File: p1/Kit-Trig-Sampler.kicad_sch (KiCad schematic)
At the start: 84 parts, among them J1 START_CV, J10 AUDIO_INR, J11 AUDIO_OUTL, J13 BANK_CV, J14 Eurorack_Power_16pin_Unshroud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, J2 LENGTH_CV, J3 SAMP_CV, J4 PITCH CV, J5 REV_TRIG, J6 PLAY_TRIG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

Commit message: changes to schem and layout
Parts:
- removed C19: 10uF_Radial_TH, 4ms_Capacitor:CP_Radial_P2.5mm, symbol 4ms_Capacitor:10uF_Radial_TH
- removed R9: 620Ω_TH0.125, 4ms_Resistor:R_Axial_DIN0207_L6.3mm_D2.5mm_P7.62mm_Horizontal, symbol 4ms_Resistor_TH:620Ω_TH0.125
- added C19: 47uF_16V_TH, 4ms_Capacitor:CP_Radial_P2.5mm, symbol 4ms_Capacitor:47uF_16V_TH
- added R35: 33k_TH0.125, 4ms_Resistor:R_Axial_DIN0207_L6.3mm_D2.5mm_P7.62mm_Horizontal, symbol 4ms_Resistor_TH:33k_TH0.125
- added R37, R9: 10k_TH0.125, 4ms_Resistor:R_Axial_DIN0207_L6.3mm_D2.5mm_P7.62mm_Horizontal, symbol 4ms_Resistor_TH:10k_TH0.125
- added unit 2 of U2
- R11: symbol 4ms_Resistor_TH:1k_TH0.125 -> 4ms_Resistor_TH:33k_TH0.125; Display 1k -> 33k; Part Number 299-1k-RC -> 299-33k-RC; Specifications 1k, 5%, 1/8W, TH0.125 -> 33k, 5%, 1/8W, TH0.125
- R13: symbol 4ms_Resistor_TH:68k_TH0.125 -> 4ms_Resistor_TH:33k_TH0.125; Display 68k -> 33k; Part Number 299-68k-RC -> 299-33k-RC; Specifications 68k, 5%, 1/8W, TH0.125 -> 33k, 5%, 1/8W, TH0.125
- R25, R26, R27: value 4.7k_TH0.125 -> 10k_TH0.125; symbol 4ms_Resistor_TH:4.7k_TH0.125 -> 4ms_Resistor_TH:10k_TH0.125; Display 4.7k -> 10k; Part Number 299-4.7k-RC -> 299-10k-RC; Specifications 4.7k, 5%, 1/8W, TH0.125 -> 10k, 5%, 1/8W, TH0.125
- U3: footprint Package_TO_SOT_THT:TO-220-3_Vertical -> 4ms_Package_TO:TO-220-3_PXO7803
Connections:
- net +12V: now also C19.1
- net GND: now also C19.2, R35.1, R9.1, U2.5 (+); no longer R13.1
- net at C3.2, R11.1, U1.5 (+): now also R37.2
- new net: R37.1, R9.2
- new net: R13.1, R35.2
- new net: U2.6 (-), U2.7
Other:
- note added: "4ms Sampler Kit"
- note removed: "4ms STS Kit"
- moved on the sheet: Bank_But1, C1, C10, C11, C12, C13, C14, C15, C16, C17, C18, C2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

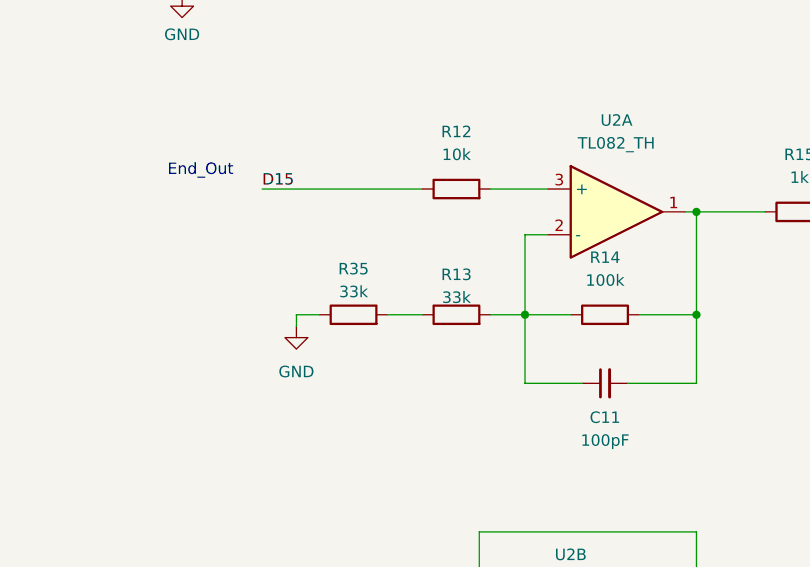
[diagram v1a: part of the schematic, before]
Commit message: Fixed R13 value (was 68k, should be 33k)
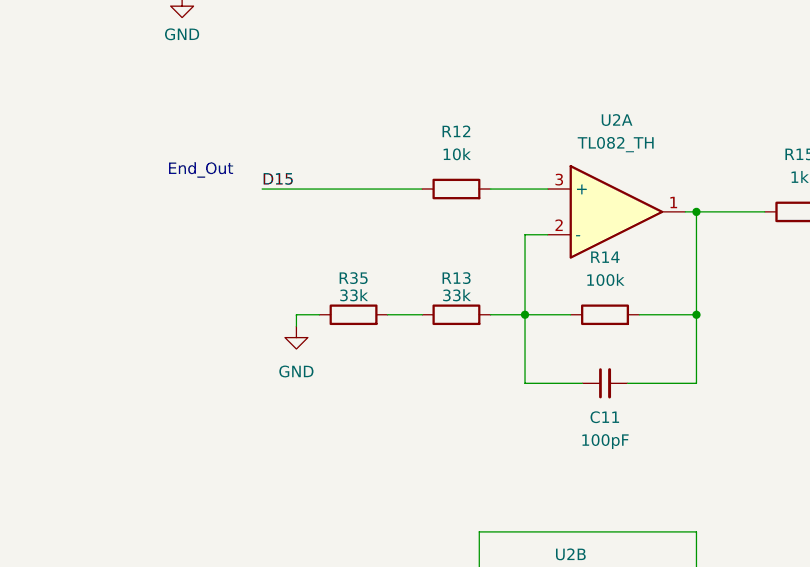
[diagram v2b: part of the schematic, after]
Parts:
- R13: value 68k_TH0.125 -> 33k_TH0.125
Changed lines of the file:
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@@
   (symbol (lib_id "4ms_Resistor_TH:33k_TH0.125") (at 203.2 129.54 90) (unit 1)
     (in_bom yes) (on_board yes) (dnp no) (fields_autoplaced)
-    (property "Reference" "R13" (at 203.2 125.095 90)
-      (effects (font (size 1.27 1.27)))
-    )
-    (property "Value" "68k_TH0.125" (at 203.2 132.08 90)
+    (property "Reference" "R13" (at 203.2 125.5141 90)
+      (effects (font (size 1.27 1.27)))
+    )
+    (property "Value" "33k_TH0.125" (at 203.2 132.08 90)
       (effects (font (size 1.27 1.27)) hide)
     )
@@
       (effects (font (size 1.27 1.27)) (justify left) hide)
     )
-    (property "Display" "33k" (at 203.2 127.635 90)
+    (property "Display" "33k" (at 203.2 127.4351 90)
       (effects (font (size 1.27 1.27)))
     )
@@
   (symbol (lib_id "4ms_Resistor_TH:33k_TH0.125") (at 191.77 129.54 90) (unit 1)
     (in_bom yes) (on_board yes) (dnp no) (fields_autoplaced)
-    (property "Reference" "R35" (at 191.77 124.46 90)
+    (property "Reference" "R35" (at 191.77 125.5141 90)
       (effects (font (size 1.27 1.27)))
     )
@@
       (effects (font (size 1.27 1.27)) (justify left) hide)
     )
-    (property "Display" "33k" (at 191.77 127 90)
-      (effects (font (size 1.27 1.27)))
-    )
+    (property "Display" "33k" (at 191.77 127.4351 90)
+      (effects (font (size 1.27 1.27)))
+    )

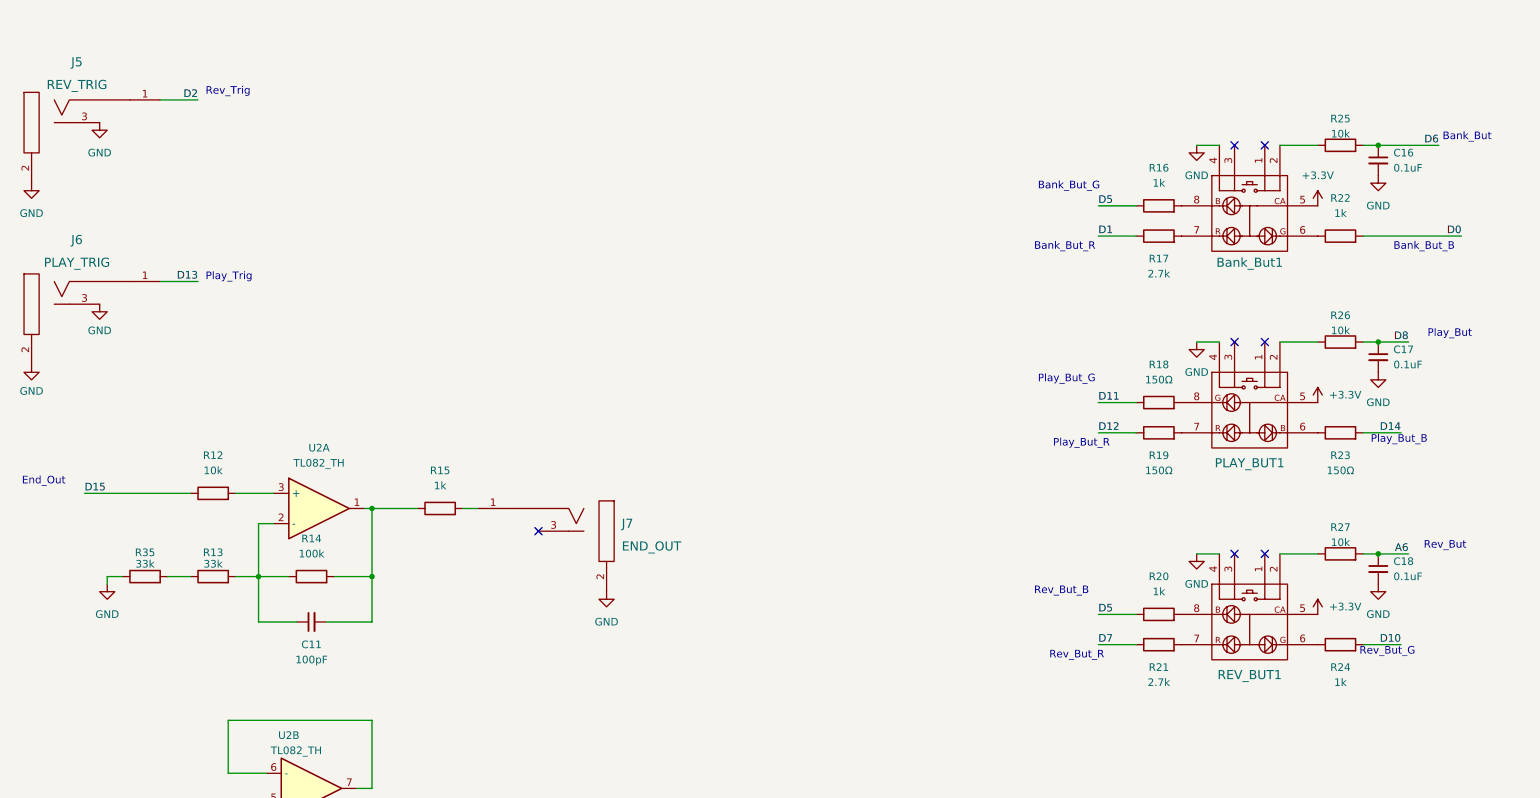
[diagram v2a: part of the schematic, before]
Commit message: Resistor Consolidation
and updates to Button LEDS
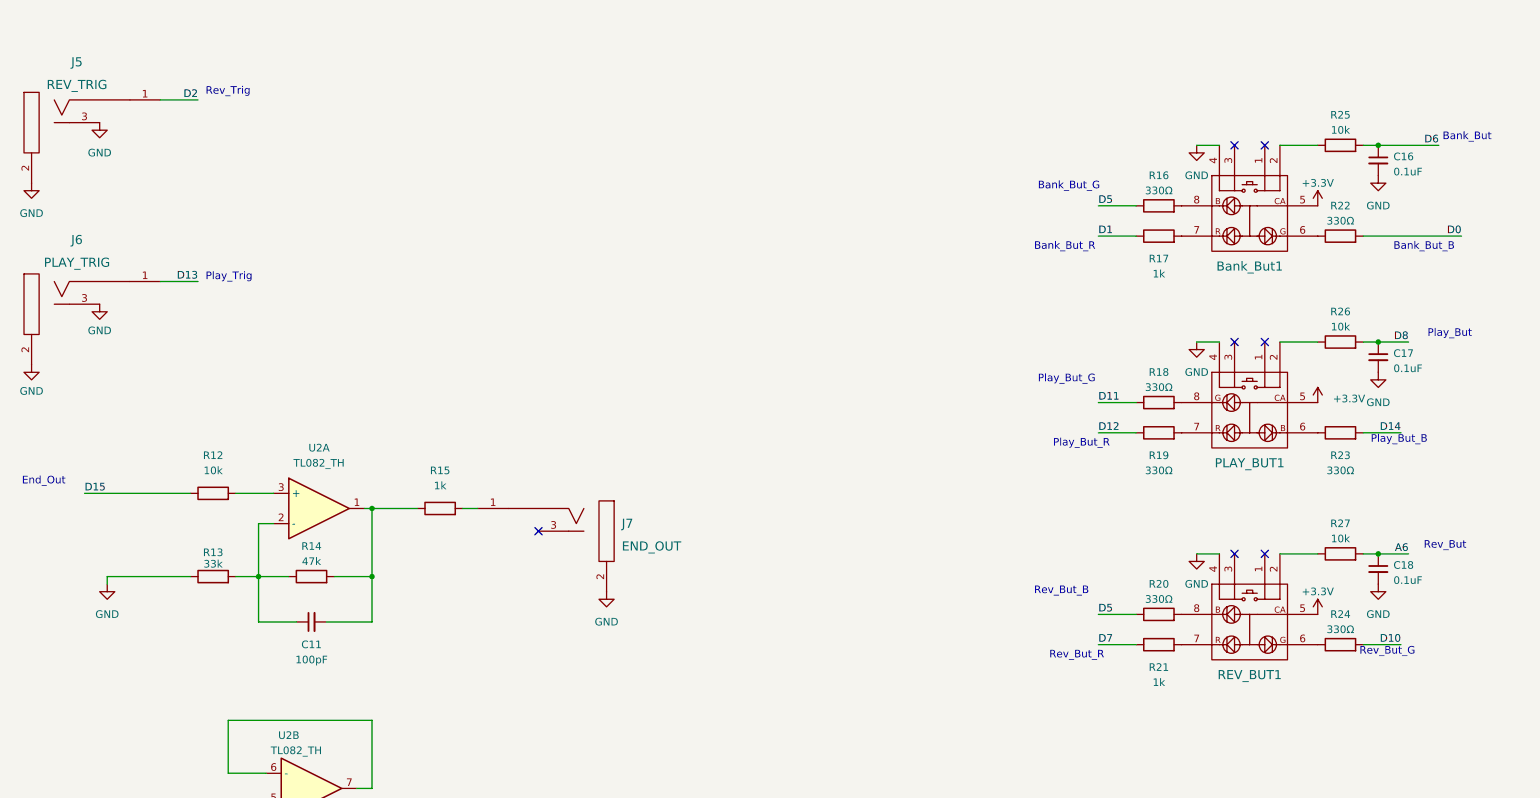
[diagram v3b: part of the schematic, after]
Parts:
- removed R35: 33k_TH0.125, 4ms_Resistor:R_Axial_DIN0207_L6.3mm_D2.5mm_P7.62mm_Horizontal, symbol 4ms_Resistor_TH:33k_TH0.125
- R14: value 100k_TH0.125 -> 47k_TH0.125; symbol 4ms_Resistor_TH:100k_TH0.125 -> 4ms_Resistor_TH:47k_TH0.125; Display 100k -> 47k; Part Number 299-100k-RC -> 299-47k-RC; Specifications 100k, 5%, 1/8W, TH0.125 -> 47k, 5%, 1/8W, TH0.125
- R16, R20, R22, R24: value 1k_TH0.125 -> 330Ω_TH0.125; symbol 4ms_Resistor_TH:1k_TH0.125 -> 4ms_Resistor_TH:330Ω_TH0.125; Display 1k -> 330Ω; Part Number 299-1k-RC -> 299-330-RC; Specifications 1k, 5%, 1/8W, TH0.125 -> 330Ω, 5%, 1/8W, TH0.125
- R17, R21: value 2.7k_TH0.125 -> 1k_TH0.125; symbol 4ms_Resistor_TH:2.7k_TH0.125 -> 4ms_Resistor_TH:1k_TH0.125; Display 2.7k -> 1k; Part Number 299-2.7k-RC -> 299-1k-RC; Specifications 2.7k, 5%, 1/8W, TH0.125 -> 1k, 5%, 1/8W, TH0.125
- R18, R19, R23: value 150Ω_TH0.125 -> 330Ω_TH0.125; symbol 4ms_Resistor_TH:150Ω_TH0.125 -> 4ms_Resistor_TH:330Ω_TH0.125; Display 150Ω -> 330Ω; Part Number 299-150-RC -> 299-330-RC; Specifications 150Ω, 5%, 1/8W, TH0.125 -> 330Ω, 5%, 1/8W, TH0.125
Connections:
- net GND: now also R13.1

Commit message: STS P2 updated to fix LED brightness issue on buttons
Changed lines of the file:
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@@
-(kicad_sch (version 20221206) (generator eeschema)
+(kicad_sch (version 20230121) (generator eeschema)
   (paper "A2")
   (junction (at 116.84 373.38) (diameter 0) (color 0 0 0 0)
@@
     (effects (font (size 1.27 1.27)) (justify left bottom))
   )
-  (text "Bank_But_G" (at 341.63 64.77 0)
+  (text "Bank_But_G" (at 405.13 74.93 0)
     (effects (font (size 1.27 1.27)) (justify left bottom))
   )
@@
     (effects (font (size 1.27 1.27)) (justify left bottom))
   )
-  (text "Bank_But_B" (at 401.32 74.93 0)
-    (effects (font (size 1.27 1.27)) (justify left bottom))
-  )
+  (text "Bank_But_B" (at 339.09 66.04 0)
+    (effects (font (size 1.27 1.27)) (justify left bottom))
+  )
